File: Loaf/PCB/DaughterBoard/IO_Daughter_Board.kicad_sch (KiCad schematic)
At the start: 12 parts, among them J1 I/O Block, J2 5V Block, J3 DB25_Socket, J4 Ground Block, J5 Ground Block, J6 Barrel Jack, SW1 SW_Push_Open, SW2 SW_Push_Open

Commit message: Updated Daughter Board
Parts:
- removed R2: 10K, Resistor_THT:R_Axial_DIN0204_L3.6mm_D1.6mm_P7.62mm_Horizontal, symbol Device:R
- removed SW1, SW2: SW_Push_Open, Button_Switch_THT:SW_PUSH_1P1T_6x3.5mm_H5.0_APEM_MJTP1250, symbol Switch:SW_Push_Open
- added J7: Screw_Terminal_01x02, AMASS_XT30UPB-M_1x02_P5.0mm_Vertical, symbol Connector:Screw_Terminal_01x02
- added SW1: SW_Push, SW_Tactile_Straight_KSL0Axx1LFTR, symbol Switch:SW_Push
- renumbered J3 to J1, J6 to J2, J1 to J3, J2 to J4, J4 to J5, J5 to J6
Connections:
- net +12V: now also J2.1; no longer J2.2
- net +5V: now also J7.1 (Pin_1), SW1.1; no longer C4.1, J1.20 (P20), J1.7
- net ESTOP: now also J7.2 (Pin_2)
- net GND: now also J2.2; no longer J2.1
- net RESET: now also SW1.2
- new net +5V Slice: C4.1, J1.20 (P20), J1.7

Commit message: See Description
Rebuilt I/O Slice daughter board.
Added transmission to the Input slice.
Got digital reading working on input slice.
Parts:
- added H1, H2, H3, H4, H5: MountingHole_Pad, MountingHole:MountingHole_3.2mm_M3_DIN965_Pad, symbol Mechanical:MountingHole_Pad
- added J8: Conn_01x02_Pin, PinHeader_1x02_P2.54mm_Horizontal, symbol Connector:Conn_01x02_Pin
- J7: footprint AMASS_XT30UPB-M_1x02_P5.0mm_Vertical -> TerminalBlock_MaiXu_MX126-5.0-02P_1x02_P5.00mm
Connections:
- net +5V: no longer J7.1 (Pin_1), SW1.1
- net +5V Slice: now also J7.2 (Pin_2), SW1.1
- net AIO0: now also J3.16 (Pin_16); no longer J3.9 (Pin_9)
- net AIO1: now also J3.15 (Pin_15); no longer J3.10 (Pin_10)
- net AIO2: now also J3.14 (Pin_14); no longer J3.11 (Pin_11)
- net AIO3: now also J3.13 (Pin_13); no longer J3.12 (Pin_12)
- net AIO4: now also J3.12 (Pin_12); no longer J3.13 (Pin_13)
- net AIO5: now also J3.11 (Pin_11); no longer J3.14 (Pin_14)
- net AIO6: now also J3.10 (Pin_10); no longer J3.15 (Pin_15)
- net AIO7: now also J3.9 (Pin_9); no longer J3.16 (Pin_16)
- net ESTOP: now also J7.1 (Pin_1); no longer J7.2 (Pin_2)
- net GND: now also H1.1, H2.1, H3.1, H4.1, H5.1
- net URX: now also J8.1 (Pin_1)
- net UTX: now also J8.2 (Pin_2)

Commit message: Added OSHE branding to VRM
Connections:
- net URX: now also J1.5, J8.2 (Pin_2); no longer J1.18 (P18), J8.1 (Pin_1)
- net UTX: now also J1.18 (P18), J8.1 (Pin_1); no longer J1.5, J8.2 (Pin_2)
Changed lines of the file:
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@@
 	)
 	(label "URX"
-		(at 52.07 74.93 0)
+		(at 52.07 72.39 0)
 		(effects
 			(font
@@
 	)
 	(label "UTX"
-		(at 36.83 58.42 180)
+		(at 36.83 55.88 180)
 		(effects
 			(font
@@
 	)
 	(label "UTX"
-		(at 52.07 72.39 0)
+		(at 52.07 74.93 0)
 		(effects
 			(font
@@
 	)
 	(label "URX"
-		(at 36.83 55.88 180)
+		(at 36.83 58.42 180)
 		(effects
 			(font

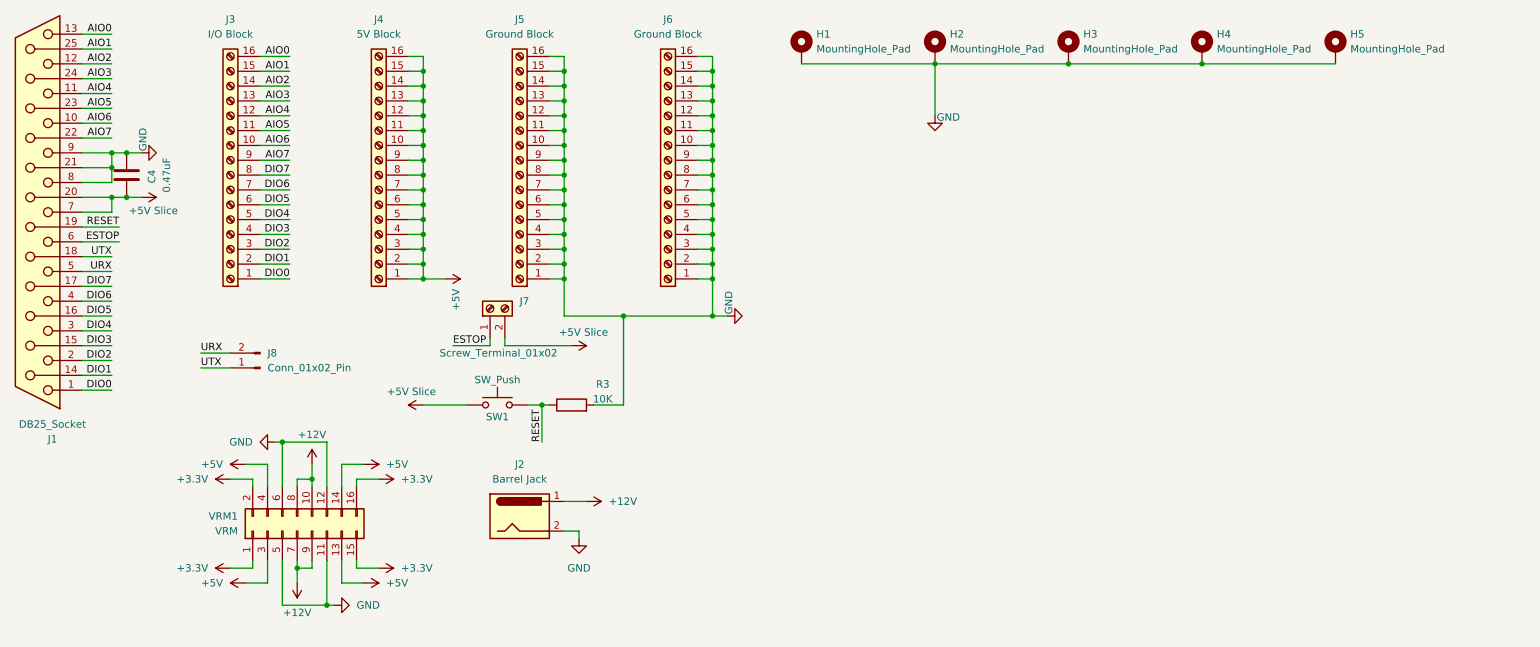
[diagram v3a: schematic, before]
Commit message: Daughter board rework for purchasable terminals
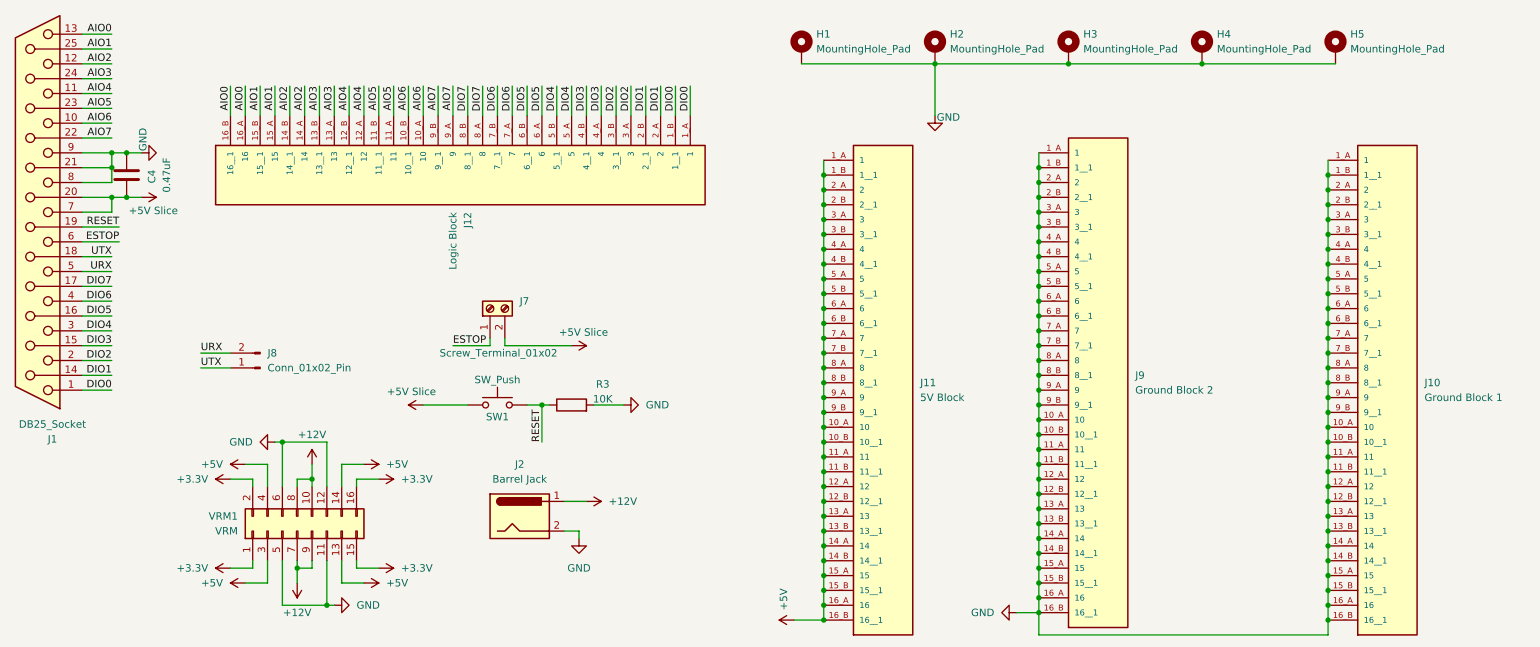
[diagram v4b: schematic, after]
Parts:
- removed J3: I/O Block, TerminalBlock:TerminalBlock_Xinya_XY308-2.54-16P_1x16_P2.54mm_Horizontal, symbol Connector:Screw_Terminal_01x16
- removed J4: 5V Block, TerminalBlock:TerminalBlock_Xinya_XY308-2.54-16P_1x16_P2.54mm_Horizontal, symbol Connector:Screw_Terminal_01x16
- removed J5, J6: Ground Block, TerminalBlock:TerminalBlock_Xinya_XY308-2.54-16P_1x16_P2.54mm_Horizontal, symbol Connector:Screw_Terminal_01x16
- added J10: Ground Block 1, TBL009-254-16GY-2GY:CUI_TBL009-254-16GY-2GY, symbol TBL009-254-16GY-2GY:TBL009-254-16GY-2GY
- added J11: 5V Block, TBL009-254-16GY-2GY:CUI_TBL009-254-16GY-2GY, symbol TBL009-254-16GY-2GY:TBL009-254-16GY-2GY
- added J12: Logic Block, TBL009-254-16GY-2GY:CUI_TBL009-254-16GY-2GY, symbol TBL009-254-16GY-2GY:TBL009-254-16GY-2GY
- added J9: Ground Block 2, TBL009-254-16GY-2GY:CUI_TBL009-254-16GY-2GY, symbol TBL009-254-16GY-2GY:TBL009-254-16GY-2GY
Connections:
- net +5V: now also J11.10_A (10), J11.10_B (10__1), J11.11_A (11), J11.11_B (11__1), J11.12_A (12), J11.12_B (12__1), J11.13_A (13), J11.13_B (13__1), J11.14_A (14), J11.14_B (14__1), J11.15_A (15), J11.15_B (15__1), J11.16_A (16), J11.16_B (16__1), J11.1_A (1), J11.1_B (1__1), J11.2_A (2), J11.2_B (2__1), J11.3_A (3), J11.3_B (3__1), J11.4_A (4), J11.4_B (4__1), J11.5_A (5), J11.5_B (5__1), J11.6_A (6), J11.6_B (6__1), J11.7_A (7), J11.7_B (7__1), J11.8_A (8), J11.8_B (8__1), J11.9_A (9), J11.9_B (9__1)
- net AIO0: now also J12.16_A (16), J12.16_B (16__1)
- net AIO1: now also J12.15_A (15), J12.15_B (15__1)
- net AIO2: now also J12.14_A (14), J12.14_B (14__1)
- net AIO3: now also J12.13_A (13), J12.13_B (13__1)
- net AIO4: now also J12.12_A (12), J12.12_B (12__1)
- net AIO5: now also J12.11_A (11), J12.11_B (11__1)
- net AIO6: now also J12.10_A (10), J12.10_B (10__1)
- net AIO7: now also J12.9_A (9), J12.9_B (9__1)
- net DIO0: now also J12.1_A (1), J12.1_B (1__1)
- net DIO1: now also J12.2_A (2), J12.2_B (2__1)
- net DIO2: now also J12.3_A (3), J12.3_B (3__1)
- net DIO3: now also J12.4_A (4), J12.4_B (4__1)
- net DIO4: now also J12.5_A (5), J12.5_B (5__1)
- net DIO5: now also J12.6_A (6), J12.6_B (6__1)
- net DIO6: now also J12.7_A (7), J12.7_B (7__1)
- net DIO7: now also J12.8_A (8), J12.8_B (8__1)
- net GND: now also J10.10_A (10), J10.10_B (10__1), J10.11_A (11), J10.11_B (11__1), J10.12_A (12), J10.12_B (12__1), J10.13_A (13), J10.13_B (13__1), J10.14_A (14), J10.14_B (14__1), J10.15_A (15), J10.15_B (15__1), J10.16_A (16), J10.16_B (16__1), J10.1_A (1), J10.1_B (1__1), J10.2_A (2), J10.2_B (2__1), J10.3_A (3), J10.3_B (3__1), J10.4_A (4), J10.4_B (4__1), J10.5_A (5), J10.5_B (5__1), J10.6_A (6), J10.6_B (6__1), J10.7_A (7), J10.7_B (7__1), J10.8_A (8), J10.8_B (8__1), J10.9_A (9), J10.9_B (9__1), J9.10_A (10), J9.10_B (10__1), J9.11_A (11), J9.11_B (11__1), J9.12_A (12), J9.12_B (12__1), J9.13_A (13), J9.13_B (13__1), J9.14_A (14), J9.14_B (14__1), J9.15_A (15), J9.15_B (15__1), J9.16_A (16), J9.16_B (16__1), J9.1_A (1), J9.1_B (1__1), J9.2_A (2), J9.2_B (2__1), J9.3_A (3), J9.3_B (3__1), J9.4_A (4), J9.4_B (4__1), J9.5_A (5), J9.5_B (5__1), J9.6_A (6), J9.6_B (6__1), J9.7_A (7), J9.7_B (7__1), J9.8_A (8), J9.8_B (8__1), J9.9_A (9), J9.9_B (9__1)
